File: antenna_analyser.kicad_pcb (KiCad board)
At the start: 2 copper layers, 100 x 50 mm, 27 parts, among them IC1 MCP6002, IC2 ARDUINO_PRO_MINI_3.3V, P1 AD9850_CONN, P2 BNC, P3 CONN_LCD, U1 AMS1117

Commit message: Final PCB
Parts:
- moved R5 18.5 mm to (146.0, 99.5), turned to 270 degrees
- moved C1 18.1 mm to (147.5, 108.0)
- moved R1 16.9 mm to (155.0, 104.5), turned to 0 degrees
- moved C5 16.1 mm to (166.5, 94.5)
- moved D1 15.4 mm to (173.0, 104.5)
- moved D2 15.2 mm to (173.0, 109.5)
- moved R4 12.2 mm to (181.0, 107.5)
- moved C6 9.85 mm to (168.5, 120.0), turned to 90 degrees
- moved C4 9.22 mm to (175.5, 114.0), turned to 0 degrees
- moved R6 7.28 mm to (177.5, 123.0)
- moved R2 5.84 mm to (164.0, 95.0)
- moved PWR1 5.22 mm to (104.5, 88.5), turned to 180 degrees
- moved P1 4.47 mm to (131.0, 110.5)
- moved P2 4.47 mm to (155.0, 94.5)
- moved R9 4.47 mm to (150.5, 122.5)
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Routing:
- net +5V: track 34.9 -> 157.1 mm
- net Net-(IC1-Pad7): track 12.5 -> 112.7 mm, vias 0 -> 1
- net GND: track 249.0 -> 343.7 mm
- net Net-(ENC1-PadA): track 0.00 -> 79.6 mm
- net Net-(ENC1-PadB): track 0.00 -> 73.5 mm
- net Net-(IC1-Pad1): track 11.7 -> 84.7 mm
- net Net-(IC2-Pad19): track 18.3 -> 50.0 mm, vias 2 -> 0
- net Net-(IC2-Pad20): track 17.8 -> 41.7 mm, vias 2 -> 0
- net Net-(IC2-Pad8): track 30.6 -> 52.4 mm
- net (no net): track 0.00 -> 21.5 mm
- net Net-(C3-Pad1): track 53.0 -> 72.0 mm
- net Net-(ENC1-PadSW2): track 92.4 -> 74.8 mm
- net Net-(IC2-Pad21): track 59.6 -> 76.5 mm, vias 0 -> 2
- net Net-(C1-Pad2): track 22.1 -> 7.46 mm
- net Net-(C5-Pad2): track 5.00 -> 14.6 mm
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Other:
- board text added: "github.com/jasiek/antenna-analyzer"

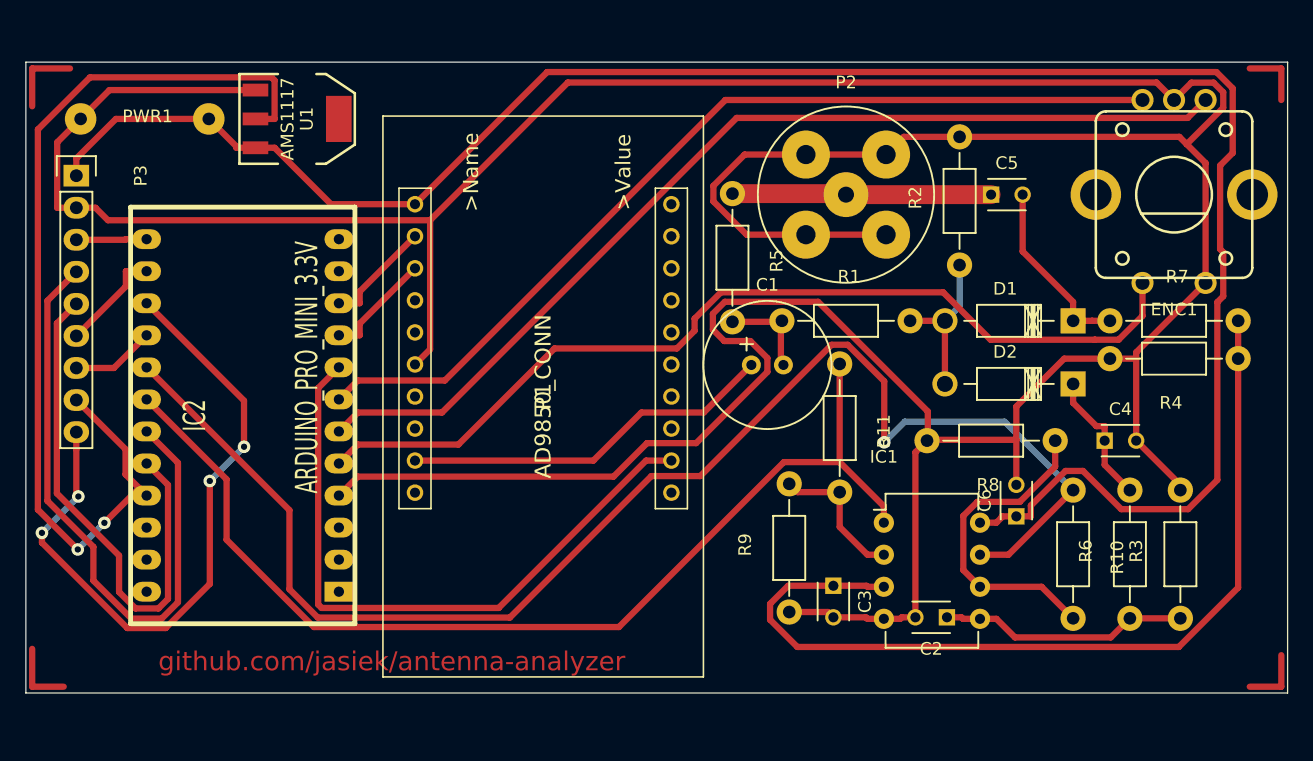
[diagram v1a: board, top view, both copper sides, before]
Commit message: Preliminary part layout
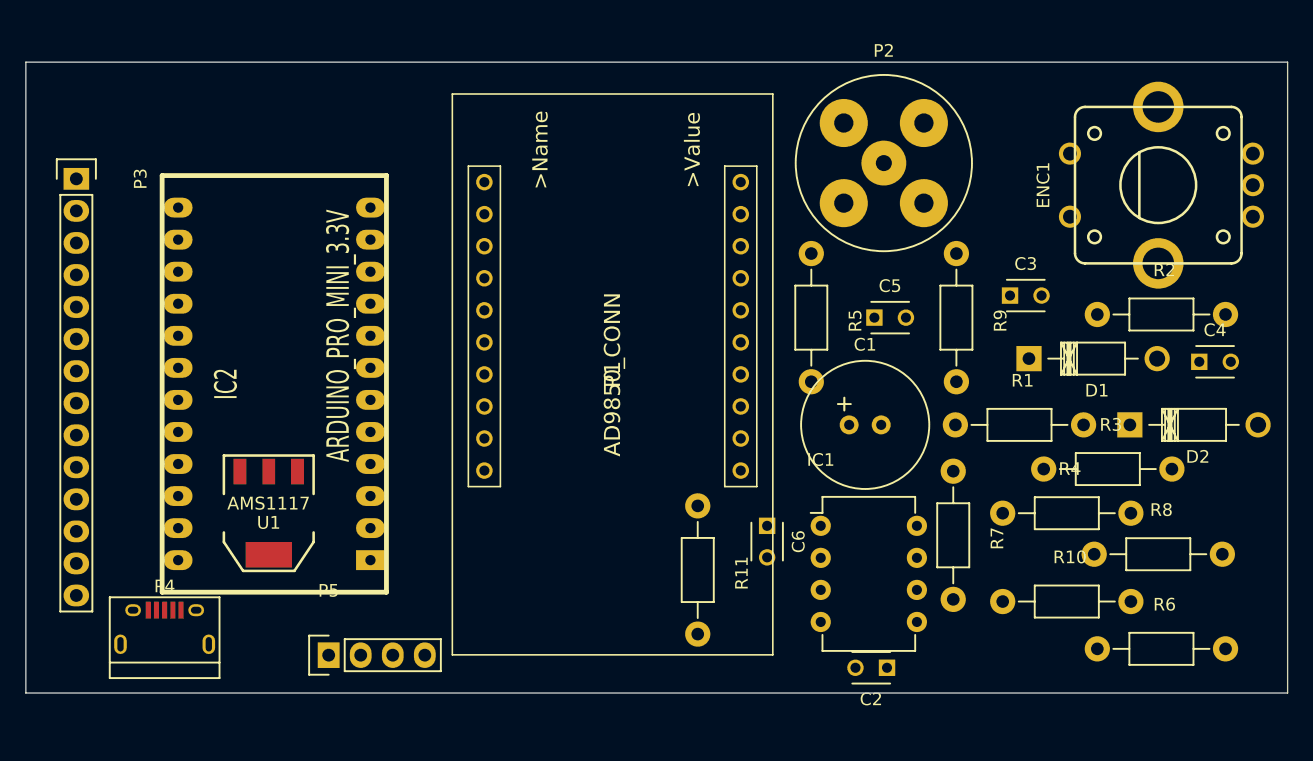
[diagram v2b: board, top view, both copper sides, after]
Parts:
- removed PWR1: CONN_01X02, Wire_Connections_Bridges:WireConnection_1mmDrill
- added P4: USB_OTG, Connect:USB_Micro-B, F.Cu at (101.0, 129.0)
- added P5: CONN_PROG, Socket_Strips:Socket_Strip_Straight_1x04, F.Cu at (114.0, 131.0)
- P3: footprint Socket_Strips:Socket_Strip_Straight_1x09 -> Socket_Strips:Socket_Strip_Straight_1x14
- moved U1 31.3 mm to (109.2, 119.8), turned to 180 degrees
- moved C3 26.9 mm to (168.0, 102.5), turned to 0 degrees
- moved R7 24.4 mm to (163.5, 121.5), turned to 270 degrees
- moved R9 22.6 mm to (163.8, 104.2), turned to 270 degrees
- moved C6 19.8 mm to (148.8, 120.8), turned to 270 degrees
- moved R2 18.4 mm to (180.0, 104.0), turned to 0 degrees
- moved R1 16.0 mm to (168.8, 112.8)
- moved R8 16.0 mm to (179.8, 123.0), turned to 0 degrees
- moved R11 15.9 mm to (143.2, 124.2)
- moved R4 14.9 mm to (172.5, 119.8), turned to 0 degrees
- moved C5 13.4 mm to (157.2, 104.2)
- moved C4 9.76 mm to (183.0, 107.8)
- moved C1 9.09 mm to (155.2, 112.8)
- moved R3 8.87 mm to (175.8, 116.2), turned to 0 degrees
- moved R6 7.91 mm to (180.0, 130.5), turned to 0 degrees
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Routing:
- net GND: track 343.7 -> 0.00 mm
- net +5V: track 157.1 -> 0.00 mm
- net Net-(IC1-Pad7): track 112.7 -> 0.00 mm, vias 1 -> 0
- net Net-(IC1-Pad1): track 84.7 -> 0.00 mm
- net Net-(ENC1-PadA): track 79.6 -> 0.00 mm
- net Net-(IC2-Pad21): track 76.5 -> 0.00 mm, vias 2 -> 0
- net Net-(ENC1-PadSW2): track 74.8 -> 0.00 mm
- net Net-(ENC1-PadB): track 73.5 -> 0.00 mm
- net Net-(C3-Pad1): track 72.0 -> 0.00 mm
- net Net-(IC2-Pad15): track 54.1 -> 0.00 mm, vias 4 -> 0
- net Net-(IC2-Pad8): track 52.4 -> 0.00 mm
- net Net-(IC2-Pad19): track 50.0 -> 0.00 mm
- net Net-(IC2-Pad20): track 41.7 -> 0.00 mm
- net Net-(C1-Pad1): track 29.8 -> 0.00 mm
- net Net-(IC1-Pad6): track 25.5 -> 0.00 mm
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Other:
- board text removed: "github.com/jasiek/antenna-analyzer"

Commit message: Two-sided PCB with a USB connector and programming pins.
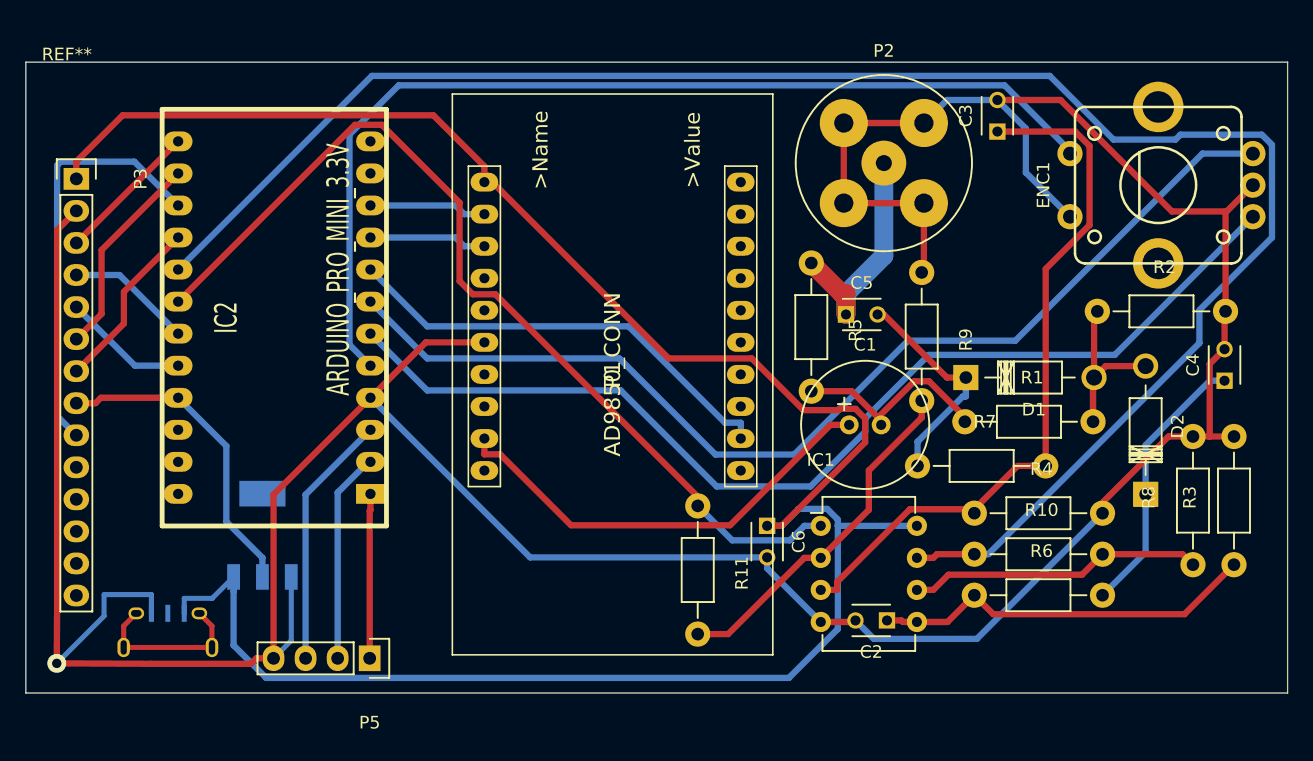
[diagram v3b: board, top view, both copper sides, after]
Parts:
- added REF**: SolderWirePad_single_2mmDrill, Wire_Pads:SolderWirePad_single_2mmDrill, F.Cu at (93.2, 87.2)
- P4, U1: moved to B.Cu
- moved C3 13.0 mm to (167.0, 89.5), turned to 90 degrees
- moved R6 10.6 mm to (170.2, 126.2)
- moved R3 10.3 mm to (185.8, 118.8), turned to 90 degrees
- moved R7 5.94 mm to (165.8, 116.0), turned to 0 degrees
- moved D2 5.64 mm to (178.8, 118.2), turned to 90 degrees
- moved IC2 5.25 mm to (113.5, 104.2)
- moved D1 5.22 mm to (164.5, 109.0)
- moved R8 5.06 mm to (182.5, 118.8), turned to 90 degrees
- moved R10 4.37 mm to (170.2, 123.0)
- moved C2 3.75 mm to (158.2, 128.2)
- moved P5 3.26 mm to (117.2, 131.2), turned to 180 degrees
- moved R9 3.13 mm to (161.0, 105.8)
- moved C4 2.50 mm to (185.0, 109.2), turned to 90 degrees
- moved C5 2.26 mm to (155.0, 104.0)
- moved R4 2.25 mm to (170.2, 119.8)
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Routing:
- net GND: track 0.00 -> 277.9 mm, vias 0 -> 1
- net +5V: track 0.00 -> 172.1 mm
- net Net-(IC1-Pad7): track 0.00 -> 143.2 mm
- net Net-(ENC1-PadB): track 0.00 -> 84.8 mm
- net Net-(ENC1-PadA): track 0.00 -> 84.4 mm
- net Net-(ENC1-PadSW2): track 0.00 -> 80.1 mm
- net Net-(IC1-Pad1): track 0.00 -> 74.9 mm
- net Net-(C3-Pad1): track 0.00 -> 57.2 mm
- net Net-(C1-Pad1): track 0.00 -> 35.8 mm
- net Net-(IC2-Pad8): track 0.00 -> 35.6 mm
- net Net-(IC2-Pad15): track 0.00 -> 33.2 mm
- net Net-(C2-Pad1): track 0.00 -> 30.7 mm
- net Net-(IC1-Pad2): track 0.00 -> 28.0 mm
- net Net-(IC2-Pad21): track 0.00 -> 25.2 mm
- net Net-(IC1-Pad6): track 0.00 -> 23.4 mm
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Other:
- net class ANT: via_dia 1 -> 1.5; via_drill 0.5 -> 1
- net class Default: trace_width 0.5 -> 0.4; via_dia 1 -> 1.5; via_drill 0.5 -> 1

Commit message: Another 2-sided PCB interation, this time with mounting points.
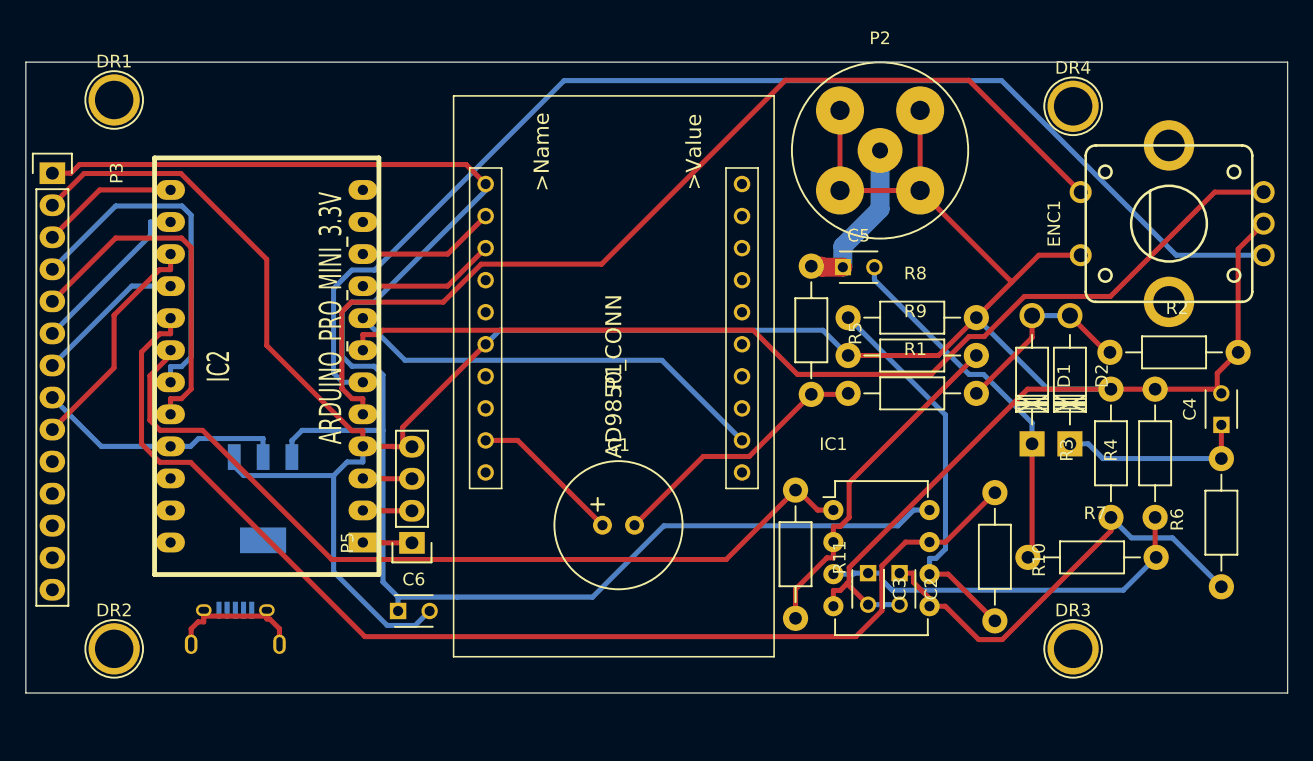
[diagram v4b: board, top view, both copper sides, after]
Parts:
- removed REF**: SolderWirePad_single_2mmDrill, Wire_Pads:SolderWirePad_single_2mmDrill
- added DR1: , Connect:1pin, F.Cu at (97.0, 87.0)
- added DR2: , Connect:1pin, F.Cu at (97.0, 130.5)
- added DR3: , Connect:1pin, F.Cu at (173.0, 130.5)
- added DR4: , Connect:1pin, F.Cu at (173.0, 87.5)
- moved C3 36.5 mm to (156.8, 124.5), turned to 270 degrees
- moved C6 30.0 mm to (119.5, 127.5), turned to 0 degrees
- moved R8 26.6 mm to (160.2, 104.2), turned to 0 degrees
- moved C1 21.1 mm to (135.7, 120.7)
- moved R6 15.6 mm to (184.8, 120.5), turned to 90 degrees
- moved R7 11.4 mm to (174.5, 123.2)
- moved R3 10.4 mm to (176.0, 115.0)
- moved R4 10.4 mm to (179.5, 115.0), turned to 90 degrees
- moved P5 9.74 mm to (120.6, 122.1), turned to 90 degrees
- moved R1 9.52 mm to (160.2, 110.2)
- moved R11 7.85 mm to (151.0, 123.0)
- moved D1 7.42 mm to (169.8, 114.2), turned to 90 degrees
- moved D2 7.21 mm to (172.8, 114.2)
- moved P4 5.36 mm to (106.6, 129.0)
- moved IC2 3.90 mm to (112.9, 108.1)
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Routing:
- net Net-(IC1-Pad7): track 143.2 -> 92.2 mm
- net +5V: track 172.1 -> 131.6 mm
- net GND: track 277.9 -> 237.5 mm, vias 1 -> 0
- net Net-(C3-Pad1): track 57.2 -> 30.8 mm
- net Net-(C1-Pad1): track 35.8 -> 12.0 mm
- net Net-(IC2-Pad19): track 10.00 -> 27.8 mm
- net Net-(IC2-Pad20): track 10.00 -> 27.8 mm
- net Net-(IC2-Pad3): track 20.2 -> 3.90 mm
- net Net-(IC2-Pad15): track 33.2 -> 18.3 mm
- net Net-(IC2-Pad2): track 16.7 -> 3.90 mm
- net Net-(C5-Pad2): track 17.8 -> 29.0 mm
- net Net-(ENC1-PadA): track 84.4 -> 95.6 mm
- net Net-(IC2-Pad1): track 13.1 -> 3.90 mm
- net Net-(IC1-Pad6): track 23.4 -> 31.1 mm
- net Net-(IC1-Pad1): track 74.9 -> 67.9 mm
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
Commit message: Straightened and simplified a couple of tracks.
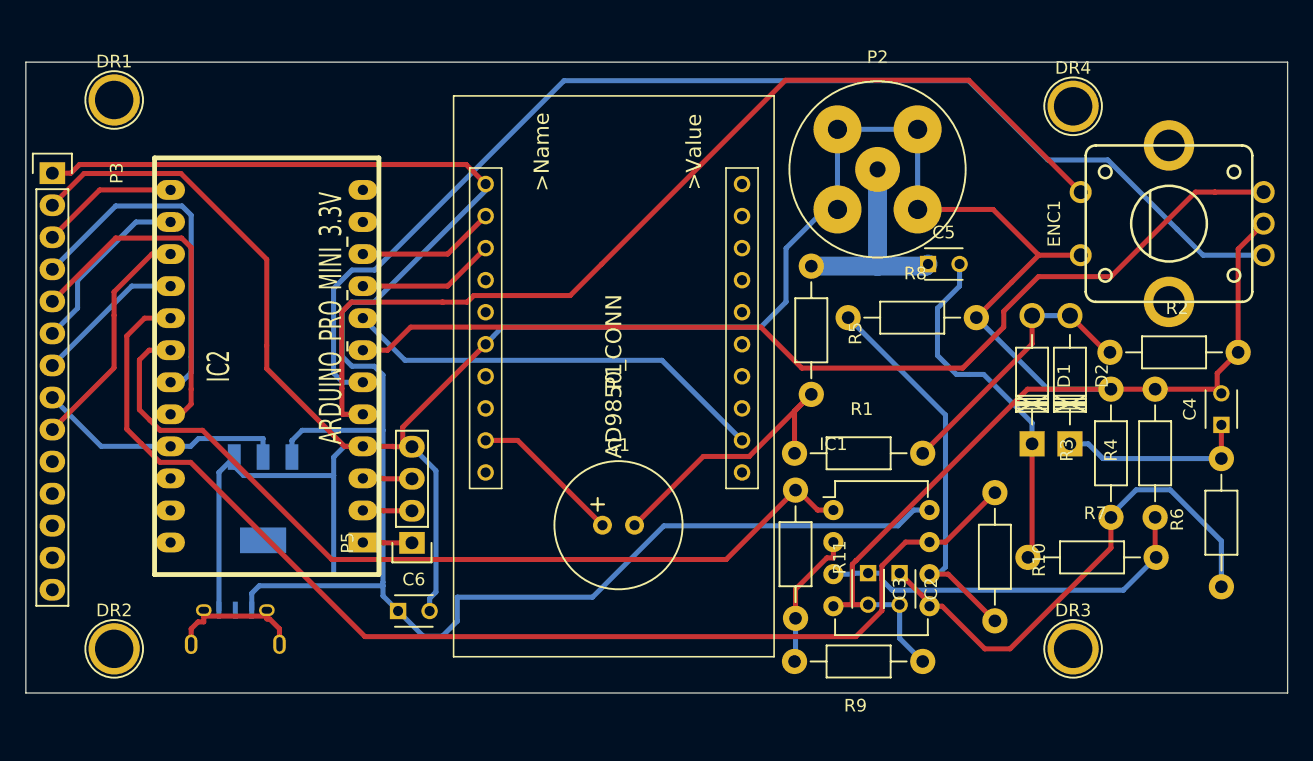
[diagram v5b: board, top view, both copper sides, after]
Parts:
- moved R9 24.6 mm to (156.0, 131.5), turned to 180 degrees
- moved C5 6.75 mm to (161.5, 100.0)
- moved R1 6.37 mm to (156.0, 115.0)
- moved P2 1.51 mm to (157.5, 92.5)
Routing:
- net Net-(IC1-Pad2): track 27.4 -> 11.0 mm
- net GND: track 237.5 -> 253.6 mm
- net +5V: track 131.6 -> 146.8 mm
- net Net-(D1-Pad2): track 15.4 -> 21.9 mm
- net Net-(C2-Pad1): track 35.6 -> 40.8 mm
- net Net-(C5-Pad1): track 13.0 -> 17.0 mm
- net Net-(C1-Pad2): track 21.3 -> 23.5 mm
- net Net-(IC1-Pad1): track 67.9 -> 70.1 mm
- net Net-(IC1-Pad7): track 92.2 -> 93.9 mm
- net Net-(IC2-Pad14): track 13.6 -> 14.3 mm
- net Net-(ENC1-PadSW2): track 79.1 -> 79.7 mm
- net Net-(C5-Pad2): track 29.0 -> 28.5 mm

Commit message: Embiggened pads on the AD9850, removed some pads to make way for tracks.
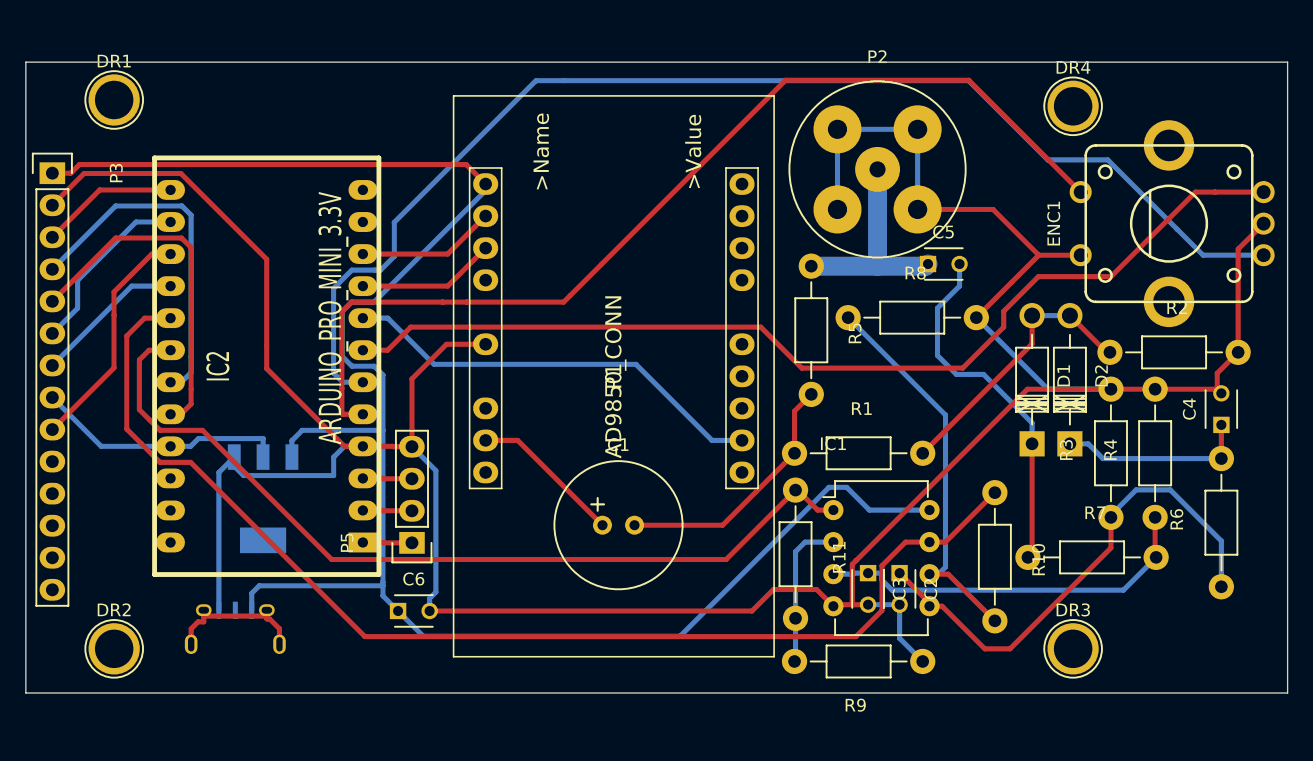
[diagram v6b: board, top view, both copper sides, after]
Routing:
- net GND: track 253.6 -> 246.9 mm
- net Net-(C1-Pad2): track 23.5 -> 20.3 mm
- net Net-(ENC1-PadA): track 95.6 -> 97.2 mm
- net Net-(IC1-Pad2): track 11.0 -> 12.0 mm
- net Net-(IC2-Pad8): track 34.3 -> 35.0 mm
